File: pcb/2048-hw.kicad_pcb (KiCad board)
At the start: 2 copper layers, 56 x 100 mm, 98 parts, among them J1 UJC-HP-3-SMT-TR, J2 Battery, J3 SWD, SW1 SW_SPDT, SW2 PUSH_A, SW3 PUSH_B, U1 STM32F303K8Tx, U2 MCP73831-2-OT, U3 AP2210N-3.3TRG1, U4 PSP_1000_JSTK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

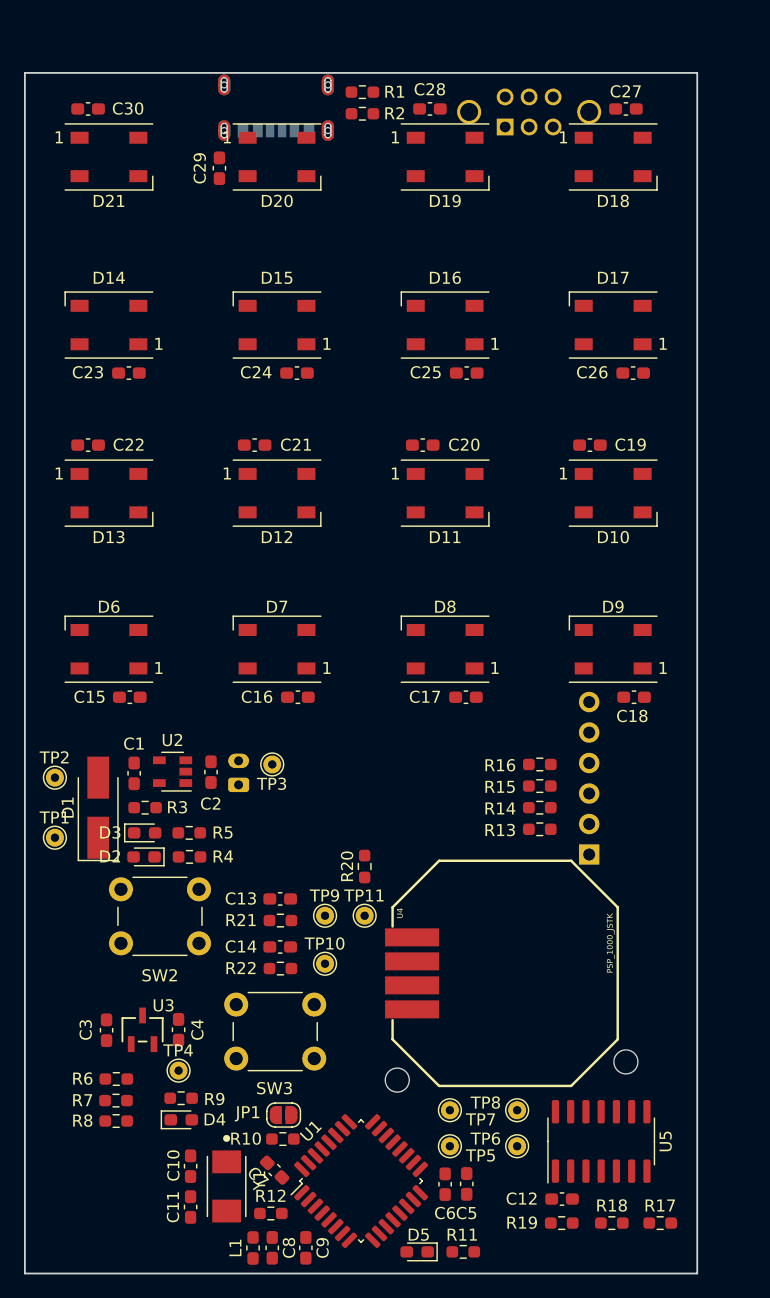
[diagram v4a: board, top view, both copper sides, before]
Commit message: Shink down PCB dimensions
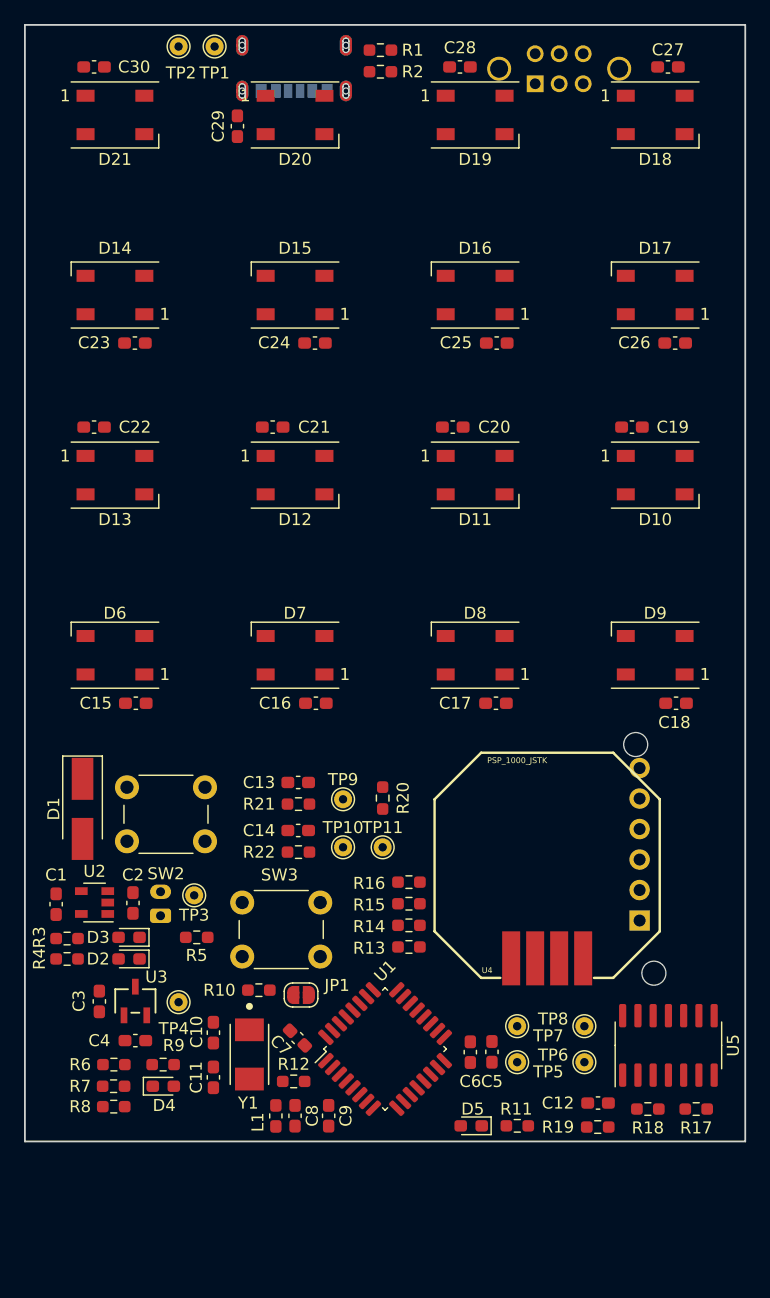
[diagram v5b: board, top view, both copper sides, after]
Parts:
- moved TP1 67.2 mm to (137.8, 57.8), turned to 270 degrees
- moved TP2 61.8 mm to (134.8, 57.8), turned to 270 degrees
- moved R13 14.7 mm to (154.0, 132.8)
- moved R16 14.7 mm to (154.0, 127.4)
- moved R14 14.7 mm to (154.0, 131.0)
- moved R15 14.7 mm to (154.0, 129.2)
- moved R4 13.3 mm to (125.5, 133.8)
- moved C1 12.7 mm to (124.6, 129.2)
- moved TP3 12.7 mm to (136.1, 128.5)
- moved U2 12.7 mm to (127.8, 129.1)
- moved C2 12.7 mm to (131.0, 129.1)
- moved J2 12.7 mm to (133.3, 130.2)
- moved R3 12.7 mm to (125.5, 132.1)
- moved R10 12.6 mm to (141.5, 136.4)
- moved D5 11.4 mm to (159.2, 147.7)
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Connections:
- D2 pad 2: +5V -> Net-(D2-Pad2)
- D3 pad 1: GND -> Net-(D3-Pad1)
- D3 pad 2: Net-(D3-Pad2) -> Net-(D2-Pad1)
- R4 pad 1: Net-(D2-Pad1) -> +5V
- R4 pad 2: Net-(R4-Pad2) -> Net-(D2-Pad2)
- R5 pad 1: Net-(D3-Pad2) -> GND
- R5 pad 2: Net-(R4-Pad2) -> Net-(D3-Pad1)
- U2 pad 1: Net-(R4-Pad2) -> Net-(D2-Pad1)
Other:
- board size 56 x 100 mm -> 60 x 93 mm

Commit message: Routing!
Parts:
- moved TP1 11.6 mm to (148.8, 61.6)
- moved TP3 5.95 mm to (131.6, 132.4)
- moved C27 5.22 mm to (172.6, 63.8)
- moved J3 4.92 mm to (171.2, 135.1)
- moved D5 4.69 mm to (156.2, 151.3)
- moved R11 4.69 mm to (160.0, 151.3)
- moved C12 4.69 mm to (166.7, 149.4)
- moved R19 4.69 mm to (166.7, 151.4)
- moved L1 4.55 mm to (139.9, 150.3), turned to 0 degrees
- moved SW1 4.47 mm to (162.5, 64.9)
- moved C1 4.47 mm to (122.6, 133.2)
- moved C10 4.47 mm to (135.7, 143.9)
- moved C11 4.47 mm to (135.7, 147.7)
- moved C13 4.47 mm to (142.8, 123.1)
- moved C14 4.47 mm to (142.8, 127.1)
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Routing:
- net V_BAT: track 0.00 -> 318.9 mm
- net GND: track 0.00 -> 212.0 mm, vias 0 -> 53
- net V_BAT_IN: track 0.00 -> 117.1 mm, vias 0 -> 3
- net +3V3: track 0.00 -> 108.0 mm, vias 0 -> 2
- net +5V: track 0.00 -> 106.9 mm, vias 0 -> 3
- net Net-(D6-Pad4): track 0.00 -> 28.9 mm, vias 0 -> 2
- net JSTK_X: track 0.00 -> 26.6 mm, vias 0 -> 3
- net BAT_ADC: track 0.00 -> 25.3 mm
- net PUSH_A: track 0.00 -> 23.7 mm
- net X_MIN: track 0.00 -> 21.1 mm
- net Net-(J3-Pad5): track 0.00 -> 21.0 mm
- net Net-(J3-Pad4): track 0.00 -> 20.7 mm
- net Net-(J3-Pad3): track 0.00 -> 20.4 mm
- net Y_MIN: track 0.00 -> 20.3 mm
- net Net-(J3-Pad2): track 0.00 -> 20.1 mm
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- added copper zone on B.Cu, net +5V
- added copper zone on F.Cu, net +5V
- added copper zone on B.Cu, net GND
- added copper zone on B.Cu, net V_BAT_IN
- added copper zone on F.Cu, net V_BAT_IN

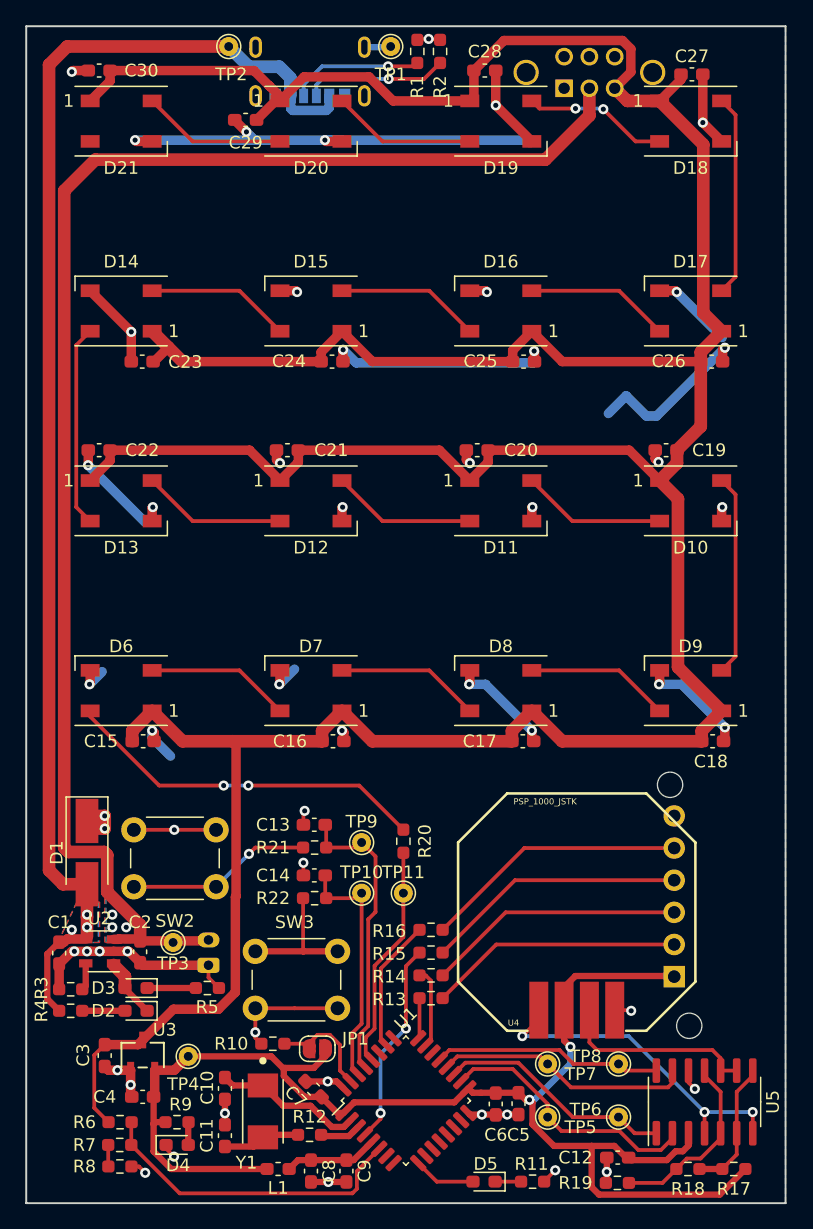
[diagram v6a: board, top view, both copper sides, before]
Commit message: Add text annotations to PCB
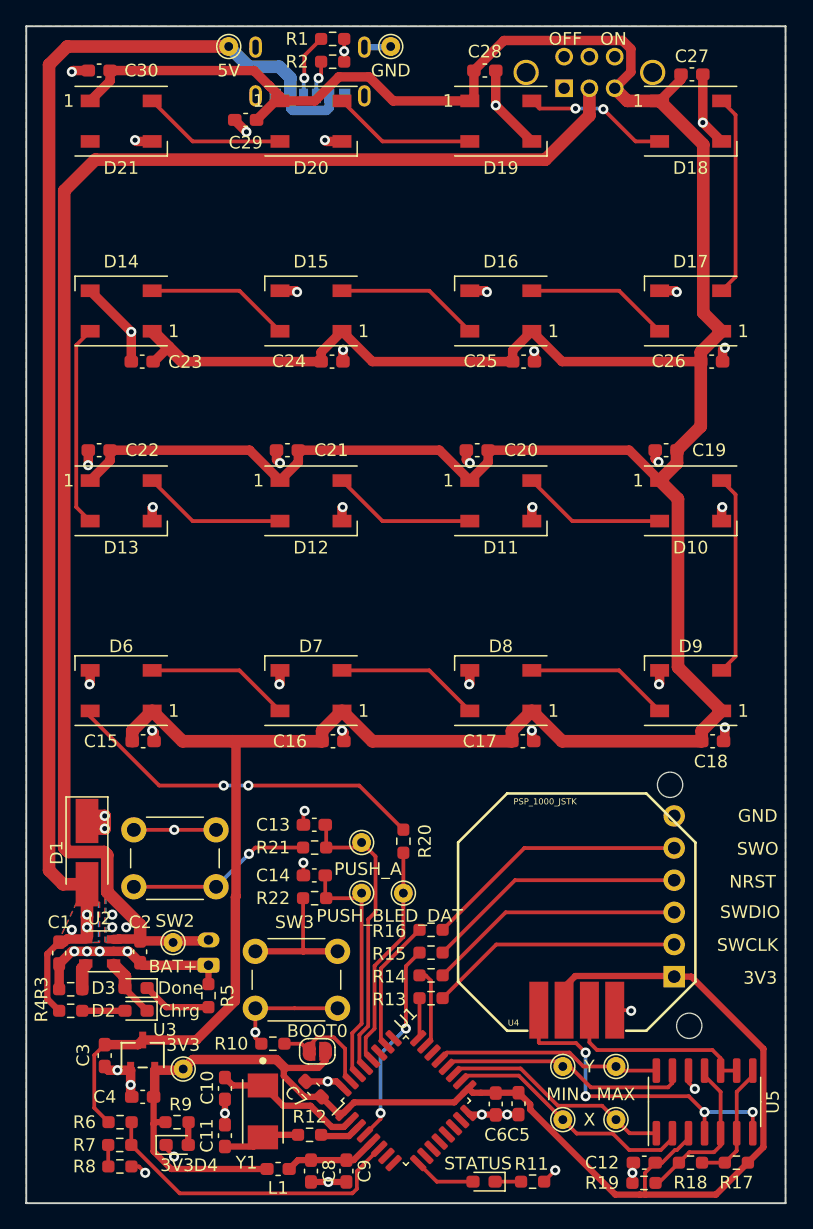
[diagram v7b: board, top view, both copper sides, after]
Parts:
- moved R2 8.53 mm to (144.2, 62.8), turned to 180 degrees
- moved R1 6.76 mm to (144.2, 61.0), turned to 180 degrees
- moved C12 2.14 mm to (168.8, 149.8)
- moved R19 2.10 mm to (168.8, 151.4)
- moved TP5 1.22 mm to (162.4, 146.4)
- moved TP7 1.22 mm to (162.4, 142.2)
- moved TP4 1.08 mm to (132.4, 142.4)
- moved R5 0.61 mm to (134.4, 136.6), turned to 270 degrees
- moved R17 0.54 mm to (176.1, 149.8)
- moved R18 0.54 mm to (172.5, 149.8)
- moved TP6 0.28 mm to (166.6, 146.4)
- moved TP8 0.28 mm to (166.6, 142.2)
- moved JP1 0.20 mm to (143.0, 141.0)
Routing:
- net GND: track 212.0 -> 116.9 mm
- net Net-(J1-PadB5): track 11.4 -> 2.86 mm
- net Net-(J1-PadA5): track 10.6 -> 5.07 mm
- net +3V3: track 108.0 -> 113.3 mm, vias 2 -> 0
- net 14_REF: track 14.6 -> 12.8 mm
- net Net-(D3-Pad1): track 3.85 -> 5.48 mm
- net X_MIN: track 21.1 -> 20.1 mm
- net 34_REF: track 10.6 -> 9.99 mm
- net JSTK_X: track 26.6 -> 27.1 mm, vias 3 -> 4
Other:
- board text added: "3V3"
- board text added: "Chrg"
- board text added: "Done"
- board text added: "GND"
- board text added: "MAX"
- board text added: "MIN"
- board text added: "NRST"
- board text added: "OFF"
- board text added: "ON"
- board text added: "SWCLK"
- board text added: "SWDIO"
- board text added: "SWO"
- board text added: "X"
- board text added: "Y"

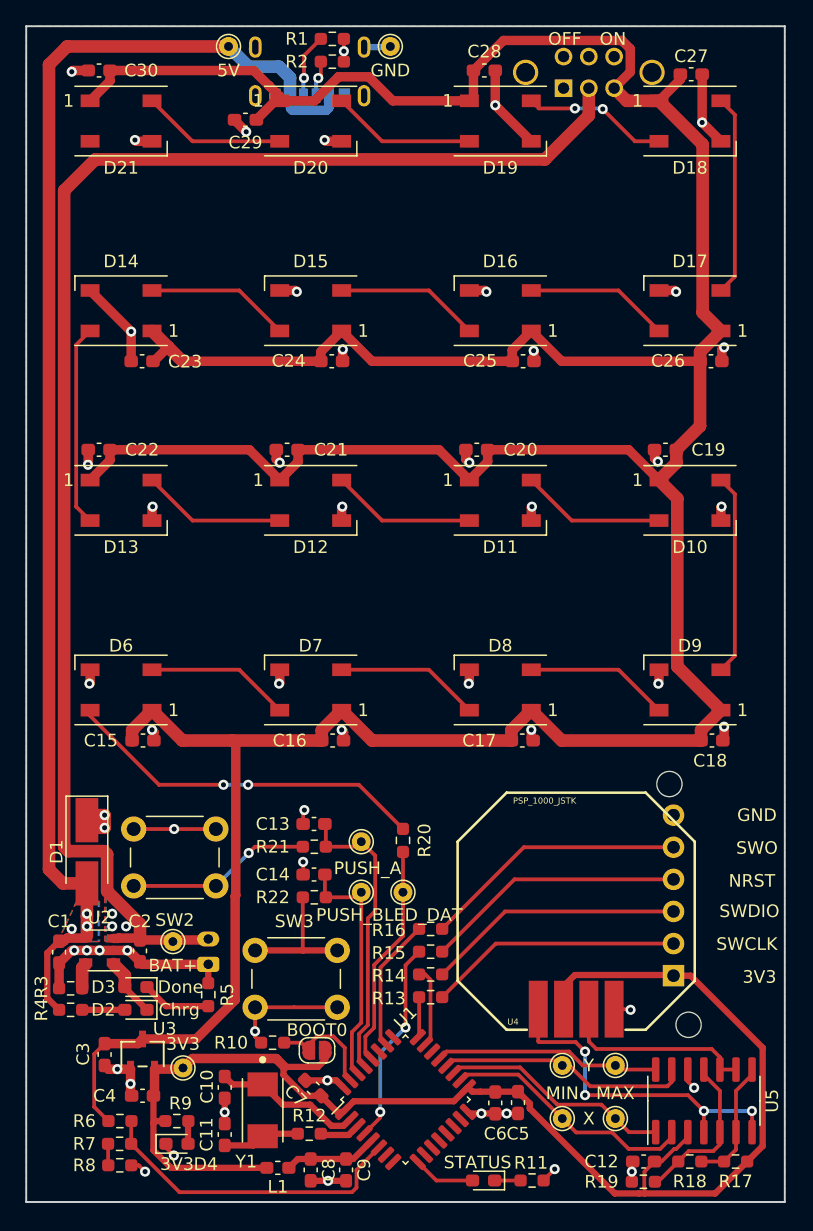
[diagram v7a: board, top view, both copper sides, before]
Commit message: Add mounting holes
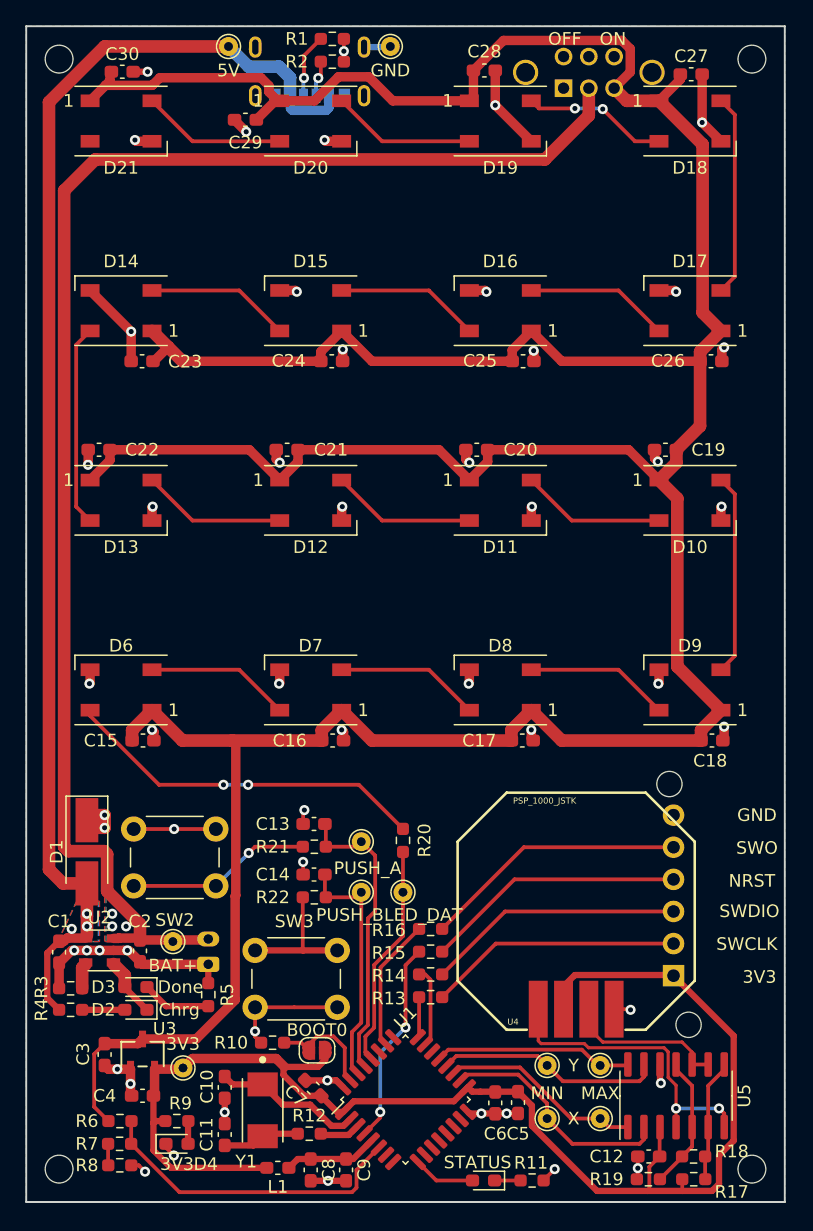
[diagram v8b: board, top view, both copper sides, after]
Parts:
- added H1: MountingHole, MountingHole:MountingHole_2.2mm_M2, F.Cu at (122.6, 62.6)
- added H2: MountingHole, MountingHole:MountingHole_2.2mm_M2, F.Cu at (122.6, 150.4)
- added H3: MountingHole, MountingHole:MountingHole_2.2mm_M2, F.Cu at (177.4, 62.6)
- added H4: MountingHole, MountingHole:MountingHole_2.2mm_M2, F.Cu at (177.4, 150.4)
- moved R17 3.60 mm to (172.8, 151.2), turned to 180 degrees
- moved U5 2.24 mm to (171.4, 144.6)
- moved C30 1.84 mm to (127.6, 63.6), turned to 0 degrees
- moved TP5 1.20 mm to (161.2, 146.4)
- moved TP7 1.20 mm to (161.2, 142.2)
- moved TP6 1.20 mm to (165.4, 146.4)
- moved TP8 1.20 mm to (165.4, 142.2)
- moved C12 0.57 mm to (169.2, 149.4)
- moved R18 0.50 mm to (172.8, 149.4)
- moved R19 0.45 mm to (169.2, 151.2)
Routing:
- net JSTK_Y: track 15.7 -> 12.7 mm
- net +3V3: track 113.3 -> 110.6 mm
- net JSTK_X: track 27.1 -> 24.4 mm, vias 4 -> 2
- net X_MAX: track 18.3 -> 15.9 mm
- net Y_MAX: track 17.9 -> 15.8 mm
- net 14_REF: track 12.8 -> 10.7 mm
- net Y_MIN: track 20.0 -> 17.9 mm
- net +5V: track 106.9 -> 105.2 mm
- net X_MIN: track 20.1 -> 18.8 mm
